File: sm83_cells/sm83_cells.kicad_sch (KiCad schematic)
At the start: 1092 parts, among them P1 PMOS, P2 PMOS, P3 PMOS, P4 PMOS

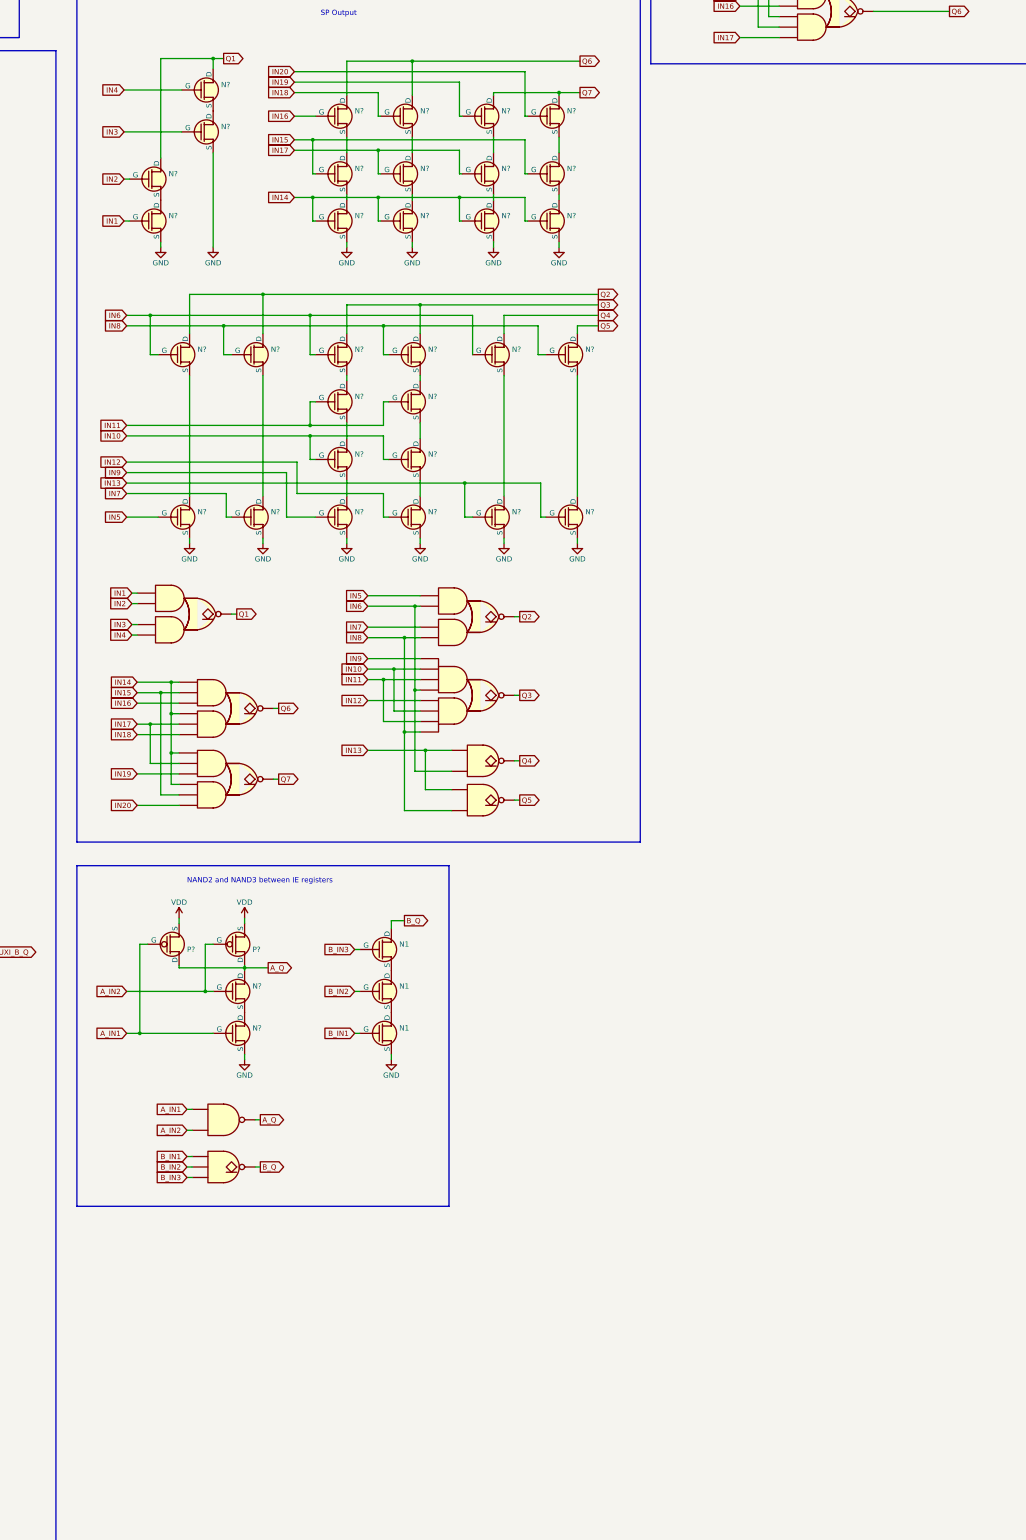
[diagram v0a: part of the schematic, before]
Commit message: Add schematic symbols for SM83 decoder 1&2 inverters
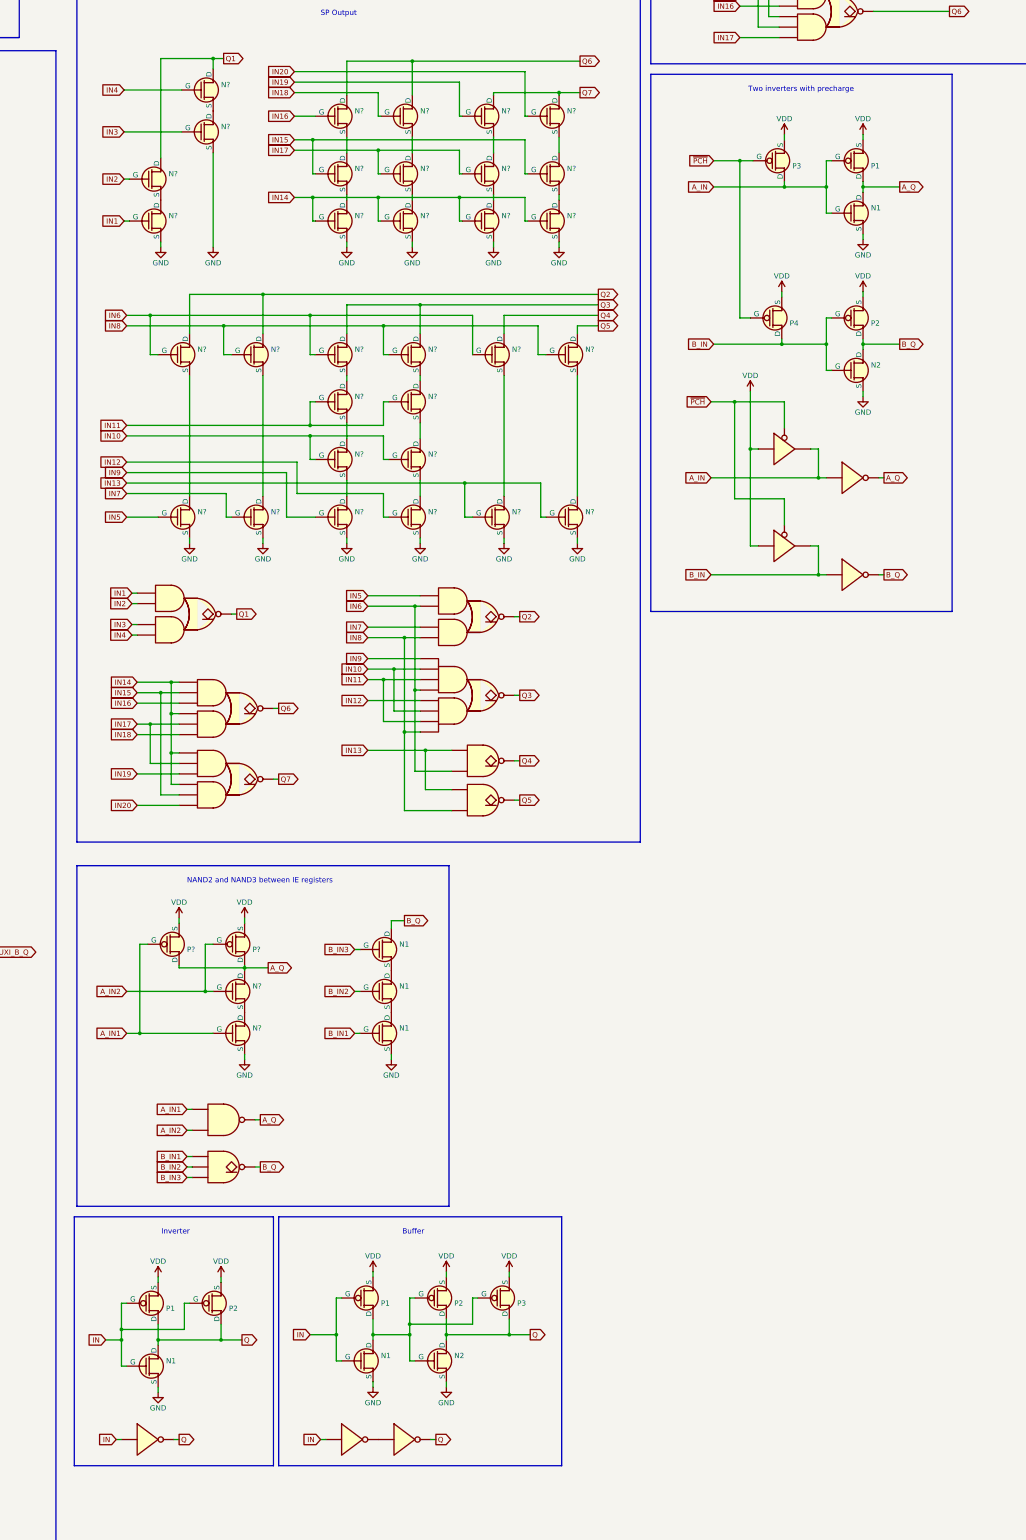
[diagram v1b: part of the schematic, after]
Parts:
- added N1 (x3), N2 (x2): NMOS, symbol DMG_CPU_Cells:NMOS
- added P1 (x3), P2 (x3), P3 (x2), P4: PMOS, symbol DMG_CPU_Cells:PMOS
- added U? (x2): TRI_BUF_IF0, symbol DMG_CPU_Cells:TRI_BUF_IF0
- added U? (x5): INVERTER_A, symbol DMG_CPU_Cells:INVERTER_A
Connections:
- net A_IN: now also N1.2 (G), P1.2 (G), P3.1 (D), U?.1, U?.4
- net A_Q: now also N1.1 (D), P1.1 (D), U?.2
- net B_IN: now also N2.2 (G), P2.2 (G), P4.1 (D), U?.1, U?.4
- net B_Q: now also N2.1 (D), P2.1 (D), U?.2
- net GND: now also N1.3 (S), N1.3 (S), N1.3 (S), N2.3 (S), N2.3 (S)
- net IN: now also N1.2 (G), N1.2 (G), P1.2 (G), P1.2 (G), P2.2 (G), U?.1, U?.1
- net Q: now also N1.1 (D), N2.1 (D), P1.1 (D), P2.1 (D), P2.1 (D), P3.1 (D), U?.2, U?.2
- net VDD: now also P1.3 (S), P1.3 (S), P1.3 (S), P2.3 (S), P2.3 (S), P2.3 (S), P3.3 (S), P3.3 (S), P4.3 (S), U?.1 (IN), U?.1 (IN), U?.3 (IN), U?.3 (IN)
- net ~{PCH}: now also P3.2 (G), P4.2 (G), U?.2 (~{ENA}), U?.2 (~{ENA})
- new net: N1.1 (D), N2.2 (G), P1.1 (D), P2.2 (G), P3.2 (G)
- new net: U?.1, U?.2
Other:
- note added: "Buffer"
- note added: "Two inverters with precharge"

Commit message: Give more meaningful names to cell types
Before this commit, many of the cells types in the chip were named in a
sloppy manner. The different inverter, latch and flip flop valiants were
just suffixed with A, B, C, D, ... Those suffixes gave no information
about the actual differences. They had to be looked up in the
documentation. Now the names of cell types with different variants have
changed:

* Inverter types are named NOT_X1, NOT_X2, NOT_X3, ... The _Xn suffix
  reflects the drive strength of the cell. X1 is the drive strength of
  the weakest inverter, X2 is double the drive strength of the weakest
  inverter.
* Flip flop types are named DFFR, DFFR_CC, DFFR_CC_Q. DFFR is a normal
  data flip flop with reset and a single clock input. The suffix _CC is
  added to flip flops that have two complementary clock inputs (CLK and
  /CLK). Flip flops that only have the positive Q output are suffixed
  with _Q.
* Latch types are named similar to flip flops: DLATCH, DLATCH_EE,
  DLATCH_EE_Q. The suffix _EE is given to latches that require
  "externally inverted enable" signals (ENA and /ENA).
* I/O pad types all start with PAD_BIDIR, PAD_IN or PAD_OUT. They also
  have suffixes that describe what makes them unique, like _PU for
  pull-ups.

Other minor changes were made to align the names with common naming
schemes of other cell libraries.
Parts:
- added N1, N2, N3, N4, N5, N6, N7: NMOS, symbol DMG_CPU_Cells:NMOS
- added P1, P2, P3, P4, P5, P6, P7: PMOS, symbol DMG_CPU_Cells:PMOS
- added U?: OR2, symbol DMG_CPU_Cells:OR2
- added U? (x3): AND2, symbol DMG_CPU_Cells:AND2
- added U?: NOT_X1, symbol DMG_CPU_Cells:NOT_X1
- U? (x48): value TRI_BUF_IF0 -> BUF_IF0; symbol DMG_CPU_Cells:TRI_BUF_IF0 -> DMG_CPU_Cells:BUF_IF0
- U? (x59): value INVERTER_A -> NOT_X1; symbol DMG_CPU_Cells:INVERTER_A -> DMG_CPU_Cells:NOT_X1
- U?: value D_LATCH_IRQ -> DLATCH_IRQ; symbol SM83_Cells:D_LATCH_IRQ -> SM83_Cells:DLATCH_IRQ
- U? (x12): value AOI_2_OD -> AOI22_OD; symbol sm83_symbols:AOI_2_OD -> sm83_symbols:AOI22_OD
- U? (x13): value AND_2 -> AND2; symbol DMG_CPU_Cells:AND_2 -> DMG_CPU_Cells:AND2
- U? (x42): value NAND_2_OD -> NAND2_OD; symbol sm83_symbols:NAND_2_OD -> sm83_symbols:NAND2_OD
- U? (x3): value AOI_1_OD -> AOI21_OD; symbol sm83_symbols:AOI_1_OD -> sm83_symbols:AOI21_OD
- U?: value DFF_ALU_FLAG -> DFFNGE_ALU_FLAG; symbol SM83_Cells:DFF_ALU_FLAG -> SM83_Cells:DFFNGE_ALU_FLAG
- U? (x12): value TRI_INV_IF1 -> NOT_IF1; symbol DMG_CPU_Cells:TRI_INV_IF1 -> DMG_CPU_Cells:NOT_IF1
- U? (x6): value NAND_2 -> NAND2; symbol DMG_CPU_Cells:NAND_2 -> DMG_CPU_Cells:NAND2
- U? (x5): value A3OI_2_OD -> AOI33_OD; symbol sm83_symbols:A3OI_2_OD -> sm83_symbols:AOI33_OD
- U?: value NAND_9_OD -> NAND9_OD; symbol sm83_symbols:NAND_9_OD -> sm83_symbols:NAND9_OD
- U? (x4): value OR_2 -> OR2; symbol DMG_CPU_Cells:OR_2 -> DMG_CPU_Cells:OR2
- U? (x3): value NOR_2 -> NOR2; symbol DMG_CPU_Cells:NOR_2 -> DMG_CPU_Cells:NOR2
- U? (x5): value TRI_INV_IF01 -> NOT_IF01; symbol sm83_symbols:TRI_INV_IF01 -> sm83_symbols:NOT_IF01
- U? (x3): value AND_3 -> AND3; symbol DMG_CPU_Cells:AND_3 -> DMG_CPU_Cells:AND3
- U? (x2): value NOR_2_OD -> NOR2_OD; symbol sm83_symbols:NOR_2_OD -> sm83_symbols:NOR2_OD
- U?: value AOI_IF1_OD -> AOI21_IF1_OD; symbol sm83_symbols:AOI_IF1_OD -> sm83_symbols:AOI21_IF1_OD
- U? (x9): value TRI_BUF_IF1 -> BUF_IF1; symbol sm83_symbols:TRI_BUF_IF1 -> sm83_symbols:BUF_IF1
- U? (x6): value TRI_INV_IF0 -> NOT_IF0; symbol DMG_CPU_Cells:TRI_INV_IF0 -> DMG_CPU_Cells:NOT_IF0
- U? (x3): value AO_2 -> AO22; symbol DMG_CPU_Cells:AO_2 -> DMG_CPU_Cells:AO22
- U?: value NAND_8_OD -> NAND8_OD; symbol sm83_symbols:NAND_8_OD -> sm83_symbols:NAND8_OD
- U?: value NAND_7_OD -> NAND7_OD; symbol sm83_symbols:NAND_7_OD -> sm83_symbols:NAND7_OD
- U?: value DFF_REG_BIT_B -> DFFGE_X2_REG_BIT; symbol SM83_Cells:DFF_REG_BIT_B -> SM83_Cells:DFFGE_X2_REG_BIT
- U? (x3): value NAND_3_OD -> NAND3_OD; symbol sm83_symbols:NAND_3_OD -> sm83_symbols:NAND3_OD
- U?: value A4OI_2_OD -> AOI44_OD; symbol sm83_symbols:A4OI_2_OD -> sm83_symbols:AOI44_OD
- U? (x2): value OA -> OA21; symbol DMG_CPU_Cells:OA -> DMG_CPU_Cells:OA21
- U? (x2): value AOI_3_OD -> AOI222_OD; symbol sm83_symbols:AOI_3_OD -> sm83_symbols:AOI222_OD
- U?: value DFF_ALU_TMP -> DFFNGE_ALU_TMP; symbol SM83_Cells:DFF_ALU_TMP -> SM83_Cells:DFFNGE_ALU_TMP
- U? (x2): value NAND_3 -> NAND3; symbol DMG_CPU_Cells:NAND_3 -> DMG_CPU_Cells:NAND3
- U?: value DFF_REG_BIT_A -> DFFGE_X1_REG_BIT; symbol SM83_Cells:DFF_REG_BIT_A -> SM83_Cells:DFFGE_X1_REG_BIT
- U?: value NAND_6_OD -> NAND6_OD; symbol sm83_symbols:NAND_6_OD -> sm83_symbols:NAND6_OD
- U?: value DSFF_REG_PC_BIT -> DFFGSE_REG_PC_BIT; symbol SM83_Cells:DSFF_REG_PC_BIT -> SM83_Cells:DFFGSE_REG_PC_BIT
- U?: value DRFF_REG_IE_BIT -> DFFGRE_REG_IE_BIT; symbol SM83_Cells:DRFF_REG_IE_BIT -> SM83_Cells:DFFGRE_REG_IE_BIT
- U? (x2): value TRI_INV_IF11 -> NOT_IF11; symbol sm83_symbols:TRI_INV_IF11 -> sm83_symbols:NOT_IF11
- U?: value DFF_REG_SP_BIT -> DFFGE_REG_SP_BIT; symbol SM83_Cells:DFF_REG_SP_BIT -> SM83_Cells:DFFGE_REG_SP_BIT
- U?: value AO_1 -> AO21; symbol DMG_CPU_Cells:AO_1 -> DMG_CPU_Cells:AO21
- U?: value DFF_REG_WZ_BIT -> DFFGE_REG_WZ_BIT; symbol SM83_Cells:DFF_REG_WZ_BIT -> SM83_Cells:DFFGE_REG_WZ_BIT
- U?: value TRI_BUF_IF11 -> BUF_IF11; symbol sm83_symbols:TRI_BUF_IF11 -> sm83_symbols:BUF_IF11
- U?: value NAND_4_OD -> NAND4_OD; symbol sm83_symbols:NAND_4_OD -> sm83_symbols:NAND4_OD
- U?: value TRI_BUF_IF00 -> BUF_IF00; symbol sm83_symbols:TRI_BUF_IF00 -> sm83_symbols:BUF_IF00
- U?: value NAND_5_OD -> NAND5_OD; symbol sm83_symbols:NAND_5_OD -> sm83_symbols:NAND5_OD
- U?: value OAI_OD -> OAI21_OD; symbol sm83_symbols:OAI_OD -> sm83_symbols:OAI21_OD
- U?: value O3AI_OD -> OAI31_OD; symbol sm83_symbols:O3AI_OD -> sm83_symbols:OAI31_OD
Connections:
- net ~{LOAD} is gone; now on net ~{ENA}: P?.2 (G), P?.2 (G), P?.2 (G), P?.2 (G), P?.2 (G), P?.2 (G), P?.2 (G)
- net ENA: now also N?.2 (G), N?.2 (G), N?.2 (G), N?.2 (G), N?.2 (G), N?.2 (G), N?.2 (G), U?. (~{ENA}), U?. (~{ENA}), U?. (~{ENA}), U?. (~{Q}), U?. (~{Q}), U?. (~{Q}), U?. (~{Q}), U?. (~{SET}), U?.1 (ENA), U?.1 (ENA), U?.1 (ENA), U?.1 (ENA), U?.1 (ENA), U?.1 (ENA), U?.1 (ENA)
- net GND: now also N1.3 (S), N4.3 (S), N6.3 (S), N7.3 (S)
- net IN1: now also N6.2 (G), N7.2 (G), P6.2 (G), P7.2 (G), U?.1, U?.1
- net IN2: now also N5.2 (G), P5.2 (G), U?.2
- net IN3: now also N4.2 (G), P4.2 (G), U?.1
- net IN4: now also N3.2 (G), P3.2 (G), U?.2
- net IN5: now also N2.2 (G), P2.2 (G), U?.2
- net Q: no longer N1.1 (D), N2.1 (D), N4.1 (D), N4.1 (D), N4.1 (D), N?.1 (D), N?.1 (D), N?.1 (D), N?.1 (D), N?.1 (D), P1.1 (D), P2.1 (D), P2.1 (D), P3.1 (D), P4.1 (D), P4.1 (D), P4.1 (D), P?.1 (D), P?.1 (D), P?.1 (D), P?.1 (D), U?., U?., U?., U?., U?.2, U?.2, U?.2, U?.2, U?.2, U?.3, U?.3, U?.4, U?.4
- net VDD: now also P1.3 (S), P2.3 (S), P5.3 (S), P6.3 (S), P7.3 (S)
- net AND_A_Q renamed AND_A_Y
- net AND_B_Q renamed AND_B_Y
- net AND_Q renamed AND_Y
- net AOI_A_~{Q} renamed AOI_A_~{Y}
- net AOI_BUF_Q renamed AOI_BUF_Y
- net AOI_B_Q renamed AOI_B_Y
- net AOI_~{Q} renamed AOI_~{Y}
- net A_Q renamed A_Y
- net B_Q renamed B_Y
- net B_Q1 renamed B_Y1
- net B_~{Q} renamed B_~{Y}
- net CHAIN_A_Q renamed CHAIN_A_Y
- net CHAIN_A_~{Q} renamed CHAIN_A_~{Y}
- net CHAIN_B_Q renamed CHAIN_B_Y
- net CHAIN_B_~{Q} renamed CHAIN_B_~{Y}
- net C_Q renamed C_Y
- net C_Q1 renamed C_Y1
- net C_~{Q} renamed C_~{Y}
- net DIST_NAND_A_Q_N renamed DIST_NAND_A_Y_N
- net DIST_NAND_A_Q_P renamed DIST_NAND_A_Y_P
- net DIST_NAND_B_Q_N renamed DIST_NAND_B_Y_N
- net DIST_NAND_B_Q_P renamed DIST_NAND_B_Y_P
- net DIST_NOR_Q_N renamed DIST_NOR_Y_N
- net DIST_NOR_Q_P renamed DIST_NOR_Y_P
- net D_Q renamed D_Y
- net D_Q1 renamed D_Y1
- net E_Q renamed E_Y
- net E_Q1 renamed E_Y1
- net H_Q1 renamed H_Y1
- net INV_A_IN renamed NOT_A_IN
- net INV_A_Q renamed NOT_A_Y
- net INV_B_IN renamed NOT_B_IN
- net INV_B_Q renamed NOT_B_Y
- net INV_IN renamed NOT_IN
- net INV_Q renamed NOT_Y
- net NOT_Y: no longer N?.1 (D), P?.1 (D), U?.2
- removed net LOAD: N?.2 (G), N?.2 (G), N?.2 (G), N?.2 (G), N?.2 (G), N?.2 (G), N?.2 (G), U?. (~{LOAD}), U?. (~{LOAD}), U?. (~{LOAD}), U?. (~{Q}), U?. (~{Q}), U?. (~{Q}), U?. (~{Q}), U?. (~{SET}), U?.1 (ENA), U?.1 (ENA), U?.1 (ENA), U?.1 (ENA), U?.1 (ENA), U?.1 (ENA), U?.1 (ENA)
- net L_Q1 renamed L_Y1
- net MUXI_A_Q renamed MUXI_A_Y
- net MUXI_B_Q renamed MUXI_B_Y
- net NAND_A_Q renamed NAND_A_Y
- net NAND_B_Q renamed NAND_B_Y
- net NAND_C_Q renamed NAND_C_Y
- net NAND_C_~{Q} renamed NAND_C_~{Y}
- net NAND_D_Q renamed NAND_D_Y
- net NAND_D_~{Q} renamed NAND_D_~{Y}
- net NAND_E_Q renamed NAND_E_Y
- net NAND_Q renamed NAND_Y
- net NOR_Q renamed NOR_Y
- net O3AI_IN_NAND_IN_AOI_A_IN2 renamed OAI31_IN_NAND_IN_AOI_A_IN2
- net O3AI_Q renamed OAI31_Y
- net OAI_IN_AOI_B_IN2 renamed OAI21_IN_AOI_B_IN2
- net OAI_Q renamed OAI21_Y
- net OR_Q renamed OR_Y
- net Q1 renamed Y1
- net Q2 renamed Y2
- net Q3 renamed Y3
- net Q4 renamed Y4
- net Q5 renamed Y5
- net Q6 renamed Y6
- net Q7 renamed Y7
- net TRI_A_IN renamed BUF_A_IN
- net TRI_A_Q renamed BUF_A_Y
- net TRI_B_IN renamed BUF_B_IN
- net TRI_B_Q renamed BUF_B_Y
- net TRI_ENA renamed BUF_ENA
- net TRI_~{ENA} renamed BUF_~{ENA}
- net Z_ENA renamed ZERO_ENA
- net Z_Q renamed ZERO_Y
- new net: N3.3 (S), N4.1 (D)
- new net: N1.2 (G), N2.1 (D), P1.2 (G), P2.1 (D), P3.1 (D), P4.1 (D)
- new net: P3.3 (S), P4.3 (S), P5.1 (D), P6.1 (D)
- new net: N2.3 (S), N3.1 (D), N5.1 (D)
- new net: U?.1, U?.3 (x2)
- new net: U?.2, U?.3
- new net: N5.3 (S), N6.1 (D)
- new net Y: N1.1 (D), N1.1 (D), N2.1 (D), N4.1 (D), N4.1 (D), N4.1 (D), N?.1 (D), N?.1 (D), N?.1 (D), N?.1 (D), N?.1 (D), P1.1 (D), P1.1 (D), P2.1 (D), P2.1 (D), P3.1 (D), P4.1 (D), P4.1 (D), P4.1 (D), P?.1 (D), P?.1 (D), P?.1 (D), P?.1 (D), U?., U?., U?., U?., U?.2, U?.2, U?.2, U?.2, U?.2, U?.3, U?.3, U?.3, U?.4, U?.4
- new net ~{IN1}: N7.1 (D), N?.1 (D), P7.1 (D), P?.1 (D), U?.2, U?.2
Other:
- note added: "AO22_AND1_TAP_IN1_N"
- note added: "OA21"
- note added: "OR2 with taps on intermediate NOR and IN1 with inverter in top center of register block"
- note added: "Y1 = !(!(IN3 & !IN4 & IN2) & !(IN3 & IN4 & !IN2)) Y2 = !(!(IN3 & !IN4 & IN2) & !IN1) Y3 = !(!IN5 & !(IN3 & IN4 & !IN2)) Y1 = (IN3 & !IN4 & IN2) | (IN3 & IN4 & !IN2) Y2 = (IN3 & !IN4 & IN2) | IN1 Y3 = IN5 | (IN3 & IN4 & !IN2)"
- note removed: "NOR2 and INVs in top center of register block"
- note removed: "OA"
- note removed: "Q1 = !(!(IN3 & !IN4 & IN2) & !(IN3 & IN4 & !IN2)) Q2 = !(!(IN3 & !IN4 & IN2) & !IN1) Q3 = !(!IN5 & !(IN3 & IN4 & !IN2)) Q1 = (IN3 & !IN4 & IN2) | (IN3 & IN4 & !IN2) Q2 = (IN3 & !IN4 & IN2) | IN1 Q3 = IN5 | (IN3 & IN4 & !IN2)"

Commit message: SM83 Layout: Add bottom part of sequencer cells
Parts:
- removed U?: OR2, symbol DMG_CPU_Cells:OR2
- removed U? (x3): AND2, symbol DMG_CPU_Cells:AND2
- added N1 (x8), N10, N11, N2 (x8), N3 (x6), N4 (x5), N5 (x4), N6 (x4), N7 (x2), N8 (x2), N9: NMOS, symbol DMG_CPU_Cells:NMOS
- added P1 (x8), P10, P11, P2 (x8), P3 (x6), P4 (x4), P5 (x4), P6 (x4), P7 (x2), P8 (x2), P9: PMOS, symbol DMG_CPU_Cells:PMOS
- added R1, R2, R?: R, symbol Device:R
- added U1, U2, U7, U? (x6): NOT_X1, symbol DMG_CPU_Cells:NOT_X1
- added U4, U6: NOT_IF1, symbol DMG_CPU_Cells:NOT_IF1
- added U5, U8: NOT_IF0, symbol DMG_CPU_Cells:NOT_IF0
- added U?: AND2, symbol DMG_CPU_Cells:AND2
- added U?: DFF_CC_Q, symbol SM83_Cells:DFF_CC_Q
- added U? (x3): OR2, symbol DMG_CPU_Cells:OR2
- added U?: BUF_IF0, symbol DMG_CPU_Cells:BUF_IF0
- added U?: OA211_IN1_N_IN3_N, symbol SM83_Cells:OA211_IN1_N_IN3_N
- added U?: NOR4_IN2_N_IN4_N, symbol SM83_Cells:NOR4_IN2_N_IN4_N
- added U?: AO33, symbol sm83_symbols:AO33
- added U?: SRLATCH_R_N, symbol SM83_Cells:SRLATCH_R_N
- added U? (x2): NOR2, symbol DMG_CPU_Cells:NOR2
- added U?: NAND2_OD, symbol sm83_symbols:NAND2_OD
- added U?: AND3, symbol DMG_CPU_Cells:AND3
- added U?: AOI331_S3, symbol SM83_Cells:AOI331_S3
- added U? (x2): NAND2, symbol DMG_CPU_Cells:NAND2
- gave numbers to parts that had none: 51
- renumbered N4 to N1, N1 to N10, N4 to N10, N4 to N11, N1 to N11, N1 to N12, N4 to N12, N1 to N13, N4 to N13, N4 to N14, N1 to N14, N1 to N15, N4 to N15, N4 to N16, N1 to N16, N1 to N17, N4 to N17, N1 to N18, N4 to N18, N4 to N19, N1 to N19, N3 to N2, N1 to N2, N4 to N2, N4 to N20, N1 to N20, N1 to N21, N1 to N22, N1 to N23, N1 to N24, N1 to N25, N1 to N26, N1 to N27, N1 to N28, N1 to N3, N2 to N3, N4 to N3, N2 to N4, N1 to N4, N4 to N5, N2 to N5, N1 to N5, N1 to N6, N1 to N7, N1 to N8, N2 to N8, N4 to N9, N1 to N9, P2 to P1, P4 to P1, P4 to P10, P2 to P11, P4 to P13, P3 to P2, P4 to P2, P1 to P3, P2 to P3, P4 to P3, P2 to P4, P1 to P4, P4 to P5, P2 to P5, P2 to P6, P1 to P6, P1 to P7, P2 to P7, P2 to P8, P4 to P9, P2 to P9
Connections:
- net CLK: now also N6.2 (G), N8.2 (G), P11.2 (G), P4.2 (G), U4.1 (ENA), U5.1 (~{ENA}), U6.1 (ENA), U8.1 (~{ENA}), U?. (Q)
- net D: now also N10.2 (G), P10.2 (G), U5.2, U?. (Q)
- net GND: now also N1.3 (S), N1.3 (S), N1.3 (S), N1.3 (S), N1.3 (S), N1.3 (S), N1.3 (S), N1.3 (S), N10.3 (S), N2.3 (S), N2.3 (S), N2.3 (S), N2.3 (S), N2.3 (S), N2.3 (S), N3.3 (S), N3.3 (S), N3.3 (S), N3.3 (S), N4.3 (S), N4.3 (S), N4.3 (S), N4.3 (S), N5.3 (S), N5.3 (S), N6.3 (S), N6.3 (S), N6.3 (S), N7.3 (S), N8.3 (S), N9.3 (S)
- net IN1: now also N1.2 (G), N1.2 (G), N1.2 (G), N1.2 (G), N1.2 (G), P1.2 (G), P1.2 (G), P1.2 (G), P1.2 (G), P1.2 (G), U?.1, U?.1, U?.1, U?.1, U?.1, U?.1
- net IN2: now also N2.2 (G), N2.2 (G), N2.2 (G), N2.2 (G), N5.2 (G), P2.2 (G), P2.2 (G), P2.2 (G), P2.2 (G), P5.2 (G), U?.2, U?.2, U?.2, U?.2, U?.2, U?.2, U?.2, U?.2
- net IN3: now also N2.2 (G), P2.2 (G), N3.2 (G), N3.2 (G), P3.2 (G), P3.2 (G), U?.3, U?.3, U?.3, U?.6; no longer N4.2 (G), P4.2 (G)
- net IN4: now also N4.2 (G), P4.2 (G), N4.2 (G), N7.2 (G), P4.2 (G), P7.2 (G), U?.2, U?.3, U?.4, U?.4, U?.4; no longer N3.2 (G), P3.2 (G)
- net IN5: now also N3.2 (G), P3.2 (G), N5.2 (G), P5.2 (G), U?.5, U?.5; no longer N2.2 (G), P2.2 (G)
- net IN6: now also N6.2 (G), P6.2 (G), U?.6
- net OR_Y: no longer N1.1 (D), P1.1 (D), U?.2
- net Q: now also N1.1 (D), N1.1 (D), N2.2 (G), P1.1 (D), P1.1 (D), P2.2 (G), U1.2, U?. (Q), U?. (Q), U?.1, U?.2
- net VDD: now also P1.3 (S), P1.3 (S), P1.3 (S), P1.3 (S), P1.3 (S), P1.3 (S), P1.3 (S), P1.3 (S), P10.3 (S), P2.3 (S), P2.3 (S), P2.3 (S), P2.3 (S), P2.3 (S), P3.3 (S), P3.3 (S), P3.3 (S), P3.3 (S), P4.3 (S), P5.3 (S), P5.3 (S), P5.3 (S), P6.3 (S), P7.3 (S), P7.3 (S), P8.3 (S), P9.3 (S), U?.1 (IN), U?.3 (IN)
- net Y: now also N1.1 (D), P1.1 (D), U?.2, N1.1 (D), N1.1 (D), N2.1 (D), N2.1 (D), N2.1 (D), N3.1 (D), N3.1 (D), N3.1 (D), N4.1 (D), N6.1 (D), N8.1 (D), P1.1 (D), P2.1 (D), P2.1 (D), P3.1 (D), P4.1 (D), P6.1 (D), P8.1 (D), U?.2, U?.3, U?.3, U?.3, U?.4, U?.5, U?.5, U?.7, U?.7
- net ~{CLK}: now also N11.2 (G), N4.2 (G), P6.2 (G), P8.2 (G)
- net ~{IN1}: now also N3.2 (G), P3.2 (G), U?.1, U?.1, U?.2; no longer N4.1 (D), N7.1 (D), P4.1 (D), P7.1 (D), U?.2, U?.2
- net NOR_Y renamed TAP_NOR
- new net: U?.1, U?.2 (x2)
- new net: U?.1, U?.3 (x4)
- new net: U1.1, U2.2, U8.2
- new net: N2.2 (G), N5.1 (D), P2.2 (G), P5.1 (D)
- new net: N1.1 (D), N2.1 (D), N3.2 (G), P2.1 (D), P3.2 (G)
- new net: P1.1 (D), P2.3 (S) (x3)
- new net: U4.2, U5.3, U6.3, U7.1
- new net: U2.1, U4.3, U8.3
- new net: N2.2 (G), N4.1 (D), N6.1 (D), P2.2 (G), P4.1 (D), P6.1 (D)
- new net: N3.1 (D), N4.3 (S)
- new net: N11.1 (D), N5.2 (G), N8.1 (D), N9.2 (G), P11.1 (D), P5.2 (G), P8.1 (D), P9.2 (G)
- new net: P10.1 (D), P11.3 (S)
- new net: P5.1 (D), P6.3 (S)
- new net: N7.1 (D), N8.2 (G), P6.1 (D), P7.1 (D), P8.2 (G)
- new net: N5.1 (D), N6.1 (D), N7.3 (S)
- new net: N1.2 (G), N2.1 (D), N3.2 (G), P1.2 (G), P2.1 (D), P3.2 (G)
- new net: U?.2, U?.2
- new net: N4.2 (G), N6.1 (D), P4.2 (G), P6.1 (D)
- new net: N10.1 (D), N11.3 (S)
- new net: N2.1 (D), N3.1 (D), N6.2 (G), P3.1 (D), P6.2 (G)
- new net: P4.1 (D), P5.1 (D), P6.3 (S)
- new net: N5.1 (D), N6.3 (S)
- new net: P7.1 (D), P8.3 (S)
- new net: U?.2, U?.3
- new net: U6.2, U7.2
- new net: P3.1 (D), P4.1 (D), P5.1 (D), P6.3 (S)
- new net: P1.1 (D), P2.1 (D), P4.3 (S), P5.3 (S)
- new net: N7.2 (G), N9.1 (D), P7.2 (G), P9.1 (D)
- new net: R?.1, U?.1, U?.3, U?.4
- new net: N2.1 (D), N3.3 (S), N5.1 (D)
- new net: N4.1 (D), N5.3 (S) (x2)
- new net: P3.1 (D), P4.3 (S) (x2)
- new net: N7.1 (D), N8.3 (S)
- new net: P2.1 (D), R2.1
- new net: N1.1 (D), N2.3 (S) (x2)
- new net: R?.2, U?.2
- new net: N1.2 (G), N3.1 (D), P1.2 (G), P3.1 (D), R1.1, R2.2
- new net: N2.1 (D), R1.2
- new net: N3.3 (S), N4.1 (D)
- new net: N1.1 (D), N4.2 (G), P1.1 (D), P4.2 (G)
- new net: P2.1 (D), P3.3 (S) (x2)
- new net SET: N4.2 (G), U?. (Q), U?.2
- new net TAP_~{IN1}: N4.1 (D), N7.1 (D), P4.1 (D), P7.1 (D), U?.2, U?.2
- new net ~{IN2}: N5.2 (G), P5.2 (G), U?.2
- new net ~{IN3}: N1.2 (G), N2.2 (G), P1.2 (G), P2.2 (G), U?.1, U?.1, U?.1, U?.3
- new net ~{IN4}: N6.2 (G), P6.2 (G), U?.4
- new net ~{RESET}: N3.2 (G), P3.2 (G), U?. (Q), U?.1, U?.2 (~{ENA})
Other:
- note added: "AO33_S3_TAP_IN1_N"
- note added: "AOI331_S3"
- note added: "DFF_CC_Q"
- note added: "NAND Gate"
- note added: "NOR Gate"
- note added: "NOR4_IN2_N_IN4_N"
- note added: "OA211_IN1_N_IN3_N"
- note added: "OR Gate"
- note added: "SRLATCH_R_N"
- note added: "Y = (!(IN1 | IN3) | (IN2 & !IN3)) & IN4 Y = ((!IN1 & !IN3) | (IN2 & !IN3)) & IN4 Y = (!IN1 | IN2) & !IN3 & IN4"
- note removed: "AO22_AND1_TAP_IN1_N"
